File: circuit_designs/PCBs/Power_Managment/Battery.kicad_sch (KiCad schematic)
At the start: 37 parts, among them J1 Switch 1, J2 Switch 2, J4 EXT_Switch, J6 MainBoard, J7 Main Board Sensors, Q3 NPN, Q4 PMOS, U1 LM2596T-ADJ, U2 TPS610333DRLR, U3 NE555P

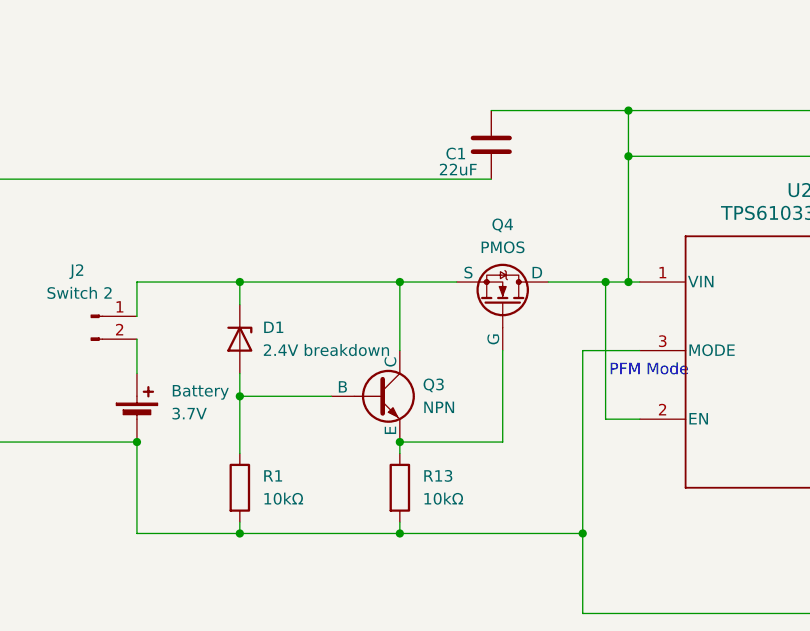
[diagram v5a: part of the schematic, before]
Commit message: fixed the low voltage protection circuit after running ltspice sims
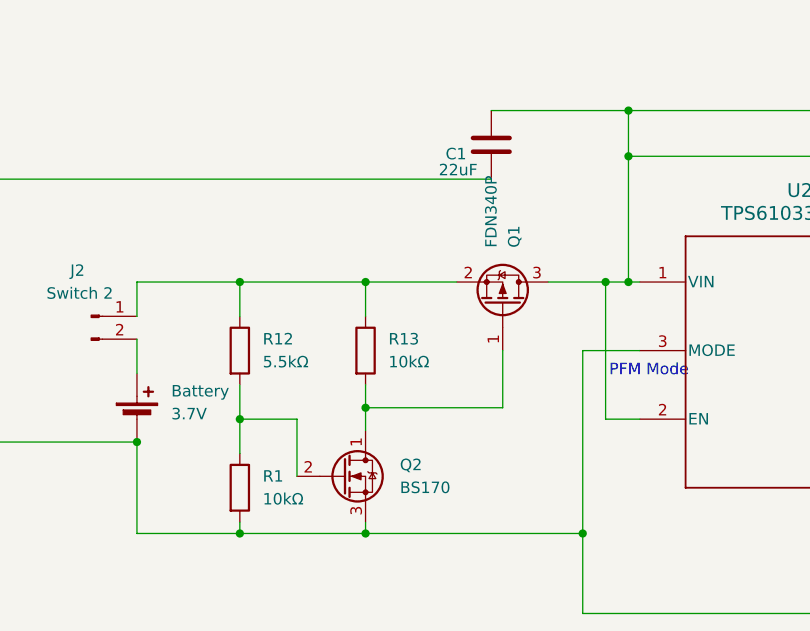
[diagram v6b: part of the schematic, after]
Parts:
- removed D1: 2.4V breakdown, Diode_THT:D_DO-41_SOD81_P10.16mm_Horizontal, symbol Diode:1N47xxA
- removed Q3: NPN, symbol Simulation_SPICE:NPN
- removed Q4: PMOS, symbol Simulation_SPICE:NMOS
- added Q1: FDN340P, Package_TO_SOT_SMD:SOT-23, symbol Transistor_FET:FDN340P
- added Q2: BS170, Package_TO_SOT_THT:TO-92_Inline, symbol Transistor_FET:BS170
- added R12: 5.5kΩ, symbol Device:R
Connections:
- net GND: now also Q2.3 (S); no longer R13.2
- net at C1.1, L2.1, U2.1 (VIN)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: now also Q1.3 (D)
- net at R13.1: now also J2.1 (Pin_1), Q1.2 (S), R12.1
- net at R1.1: now also Q2.2 (G), R12.2
- new net: Q1.1 (G), Q2.1 (D), R13.2
